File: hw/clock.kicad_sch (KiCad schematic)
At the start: 63 parts, among them J1 USB-A1HSW6, J2 USB-A1HSW6, J3 USB-A1HSW6, SW1 TL3305AF260QG, SW2 TL3305AF260QG, SW3 TL3305AF260QG, U1 LPC812M101JDH20, U10 HDSP-5321 Common Anode, U11 HDSP-5321 Common Anode, U12 HDSP-5321 Common Anode, U13 MCP9808T-E/MS, U14 AP2192ASG-13, U15 INA219AIDR, U16 INA219AIDR, U2 INTERFACE-FT230XS-R_SSOP16_, U3 SN74HC595DR, U4 SN74HC595DR, U5 SN74HC595DR, U6 SN74HC595DR, U7 SN74HC595DR, U8 SN74HC595DR, U9 MCP7940MT-I_SN, Y1 30MHz, Y2 32.768KHz

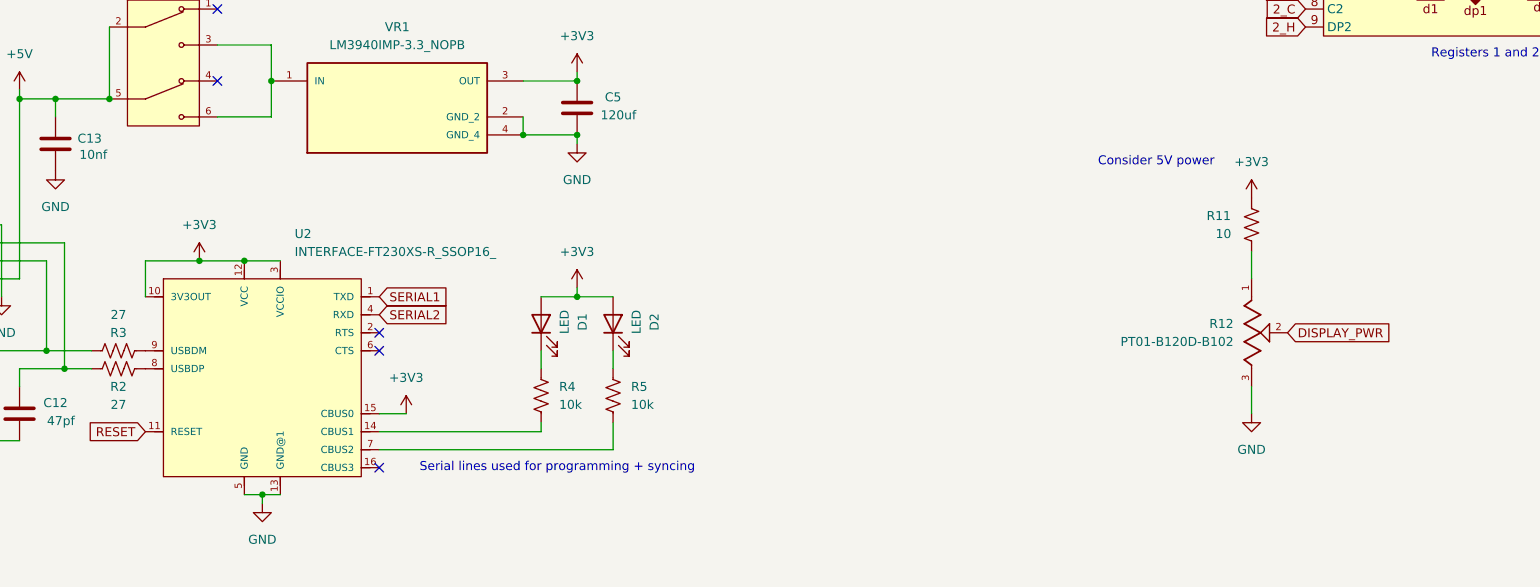
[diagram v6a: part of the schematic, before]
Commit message: Add safety resistors and 5v display backup supply
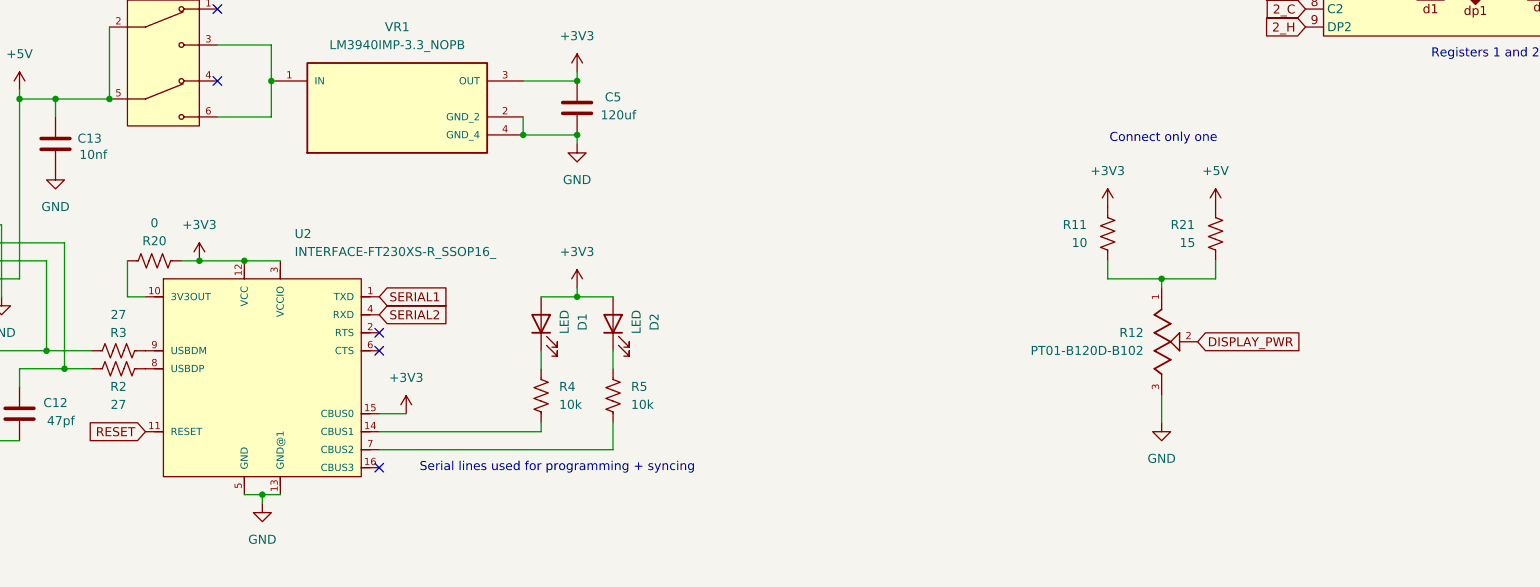
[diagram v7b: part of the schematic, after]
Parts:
- added R20: 0, Resistor_SMD:R_0805_2012Metric, symbol Device:R_US
- added R21: 15, Resistor_SMD:R_0805_2012Metric, symbol Device:R_US
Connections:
- net +3V3: now also R20.2; no longer U2.10 (3V3OUT)
- net +5V: now also R21.2
- net at R11.1, R12.1: now also R21.1
- new net: R20.1, U2.10 (3V3OUT)
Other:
- note added: "Connect only one"
- note removed: "Consider 5V power"
- moved on the sheet: R11, R12

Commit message: Change passives
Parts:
- C1, C2: value 18pf -> 16pf
- C13: value 10nf -> 1uf
- C3, C4: value 12.5pf -> 19pf
- C5, C8, C9: value 120uf -> 100uf
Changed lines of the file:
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@@
 			)
 		)
-		(property "Value" "120uf"
+		(property "Value" "100uf"
 			(at 150.368 126.746 0)
 			(effects
@@
 			)
 		)
-		(property "Value" "120uf"
+		(property "Value" "100uf"
 			(at 159.512 216.916 0)
 			(effects
@@
 			)
 		)
-		(property "Value" "18pf"
+		(property "Value" "16pf"
 			(at 123.19 69.596 90)
 			(effects
@@
 			)
 		)
-		(property "Value" "120uf"
+		(property "Value" "100uf"
 			(at 150.368 144.526 0)
 			(effects
@@
 			)
 		)
-		(property "Value" "12.5pf"
+		(property "Value" "19pf"
 			(at 212.09 67.056 90)
 			(effects
@@
 			)
 		)
-		(property "Value" "10nf"
+		(property "Value" "1uf"
 			(at 85.344 222.504 0)
 			(effects
@@
 			)
 		)
-		(property "Value" "12.5pf"
+		(property "Value" "19pf"
 			(at 232.41 67.056 90)
 			(effects
@@
 			)
 		)
-		(property "Value" "18pf"
+		(property "Value" "16pf"
 			(at 146.05 69.596 90)
 			(effects
